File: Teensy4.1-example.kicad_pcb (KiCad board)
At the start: 4 copper layers, 61.5 x 47.5 mm, 80 parts, among them IC1 MIMXRT1062DVJ6B, J1 Conn_01x11_Male, J2 Conn_01x11_Male, J3 Conn_01x12_Male, J4 Conn_01x11_Male, J5 Conn_01x11_Male, J6 Conn_01x03_Male, J7 Conn_01x03_Male, P2 D26, Q1 Q_PMOS_GDS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

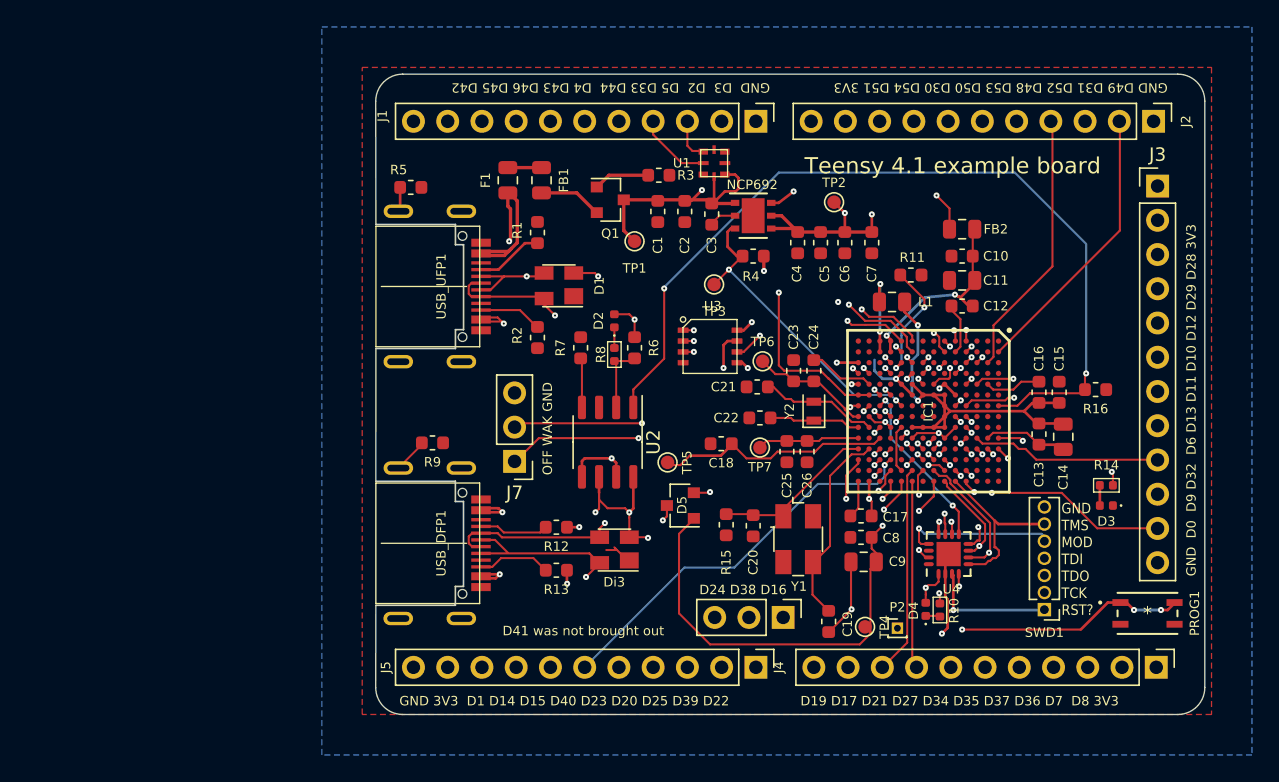
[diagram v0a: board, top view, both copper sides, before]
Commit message: add ARJP11B magjack
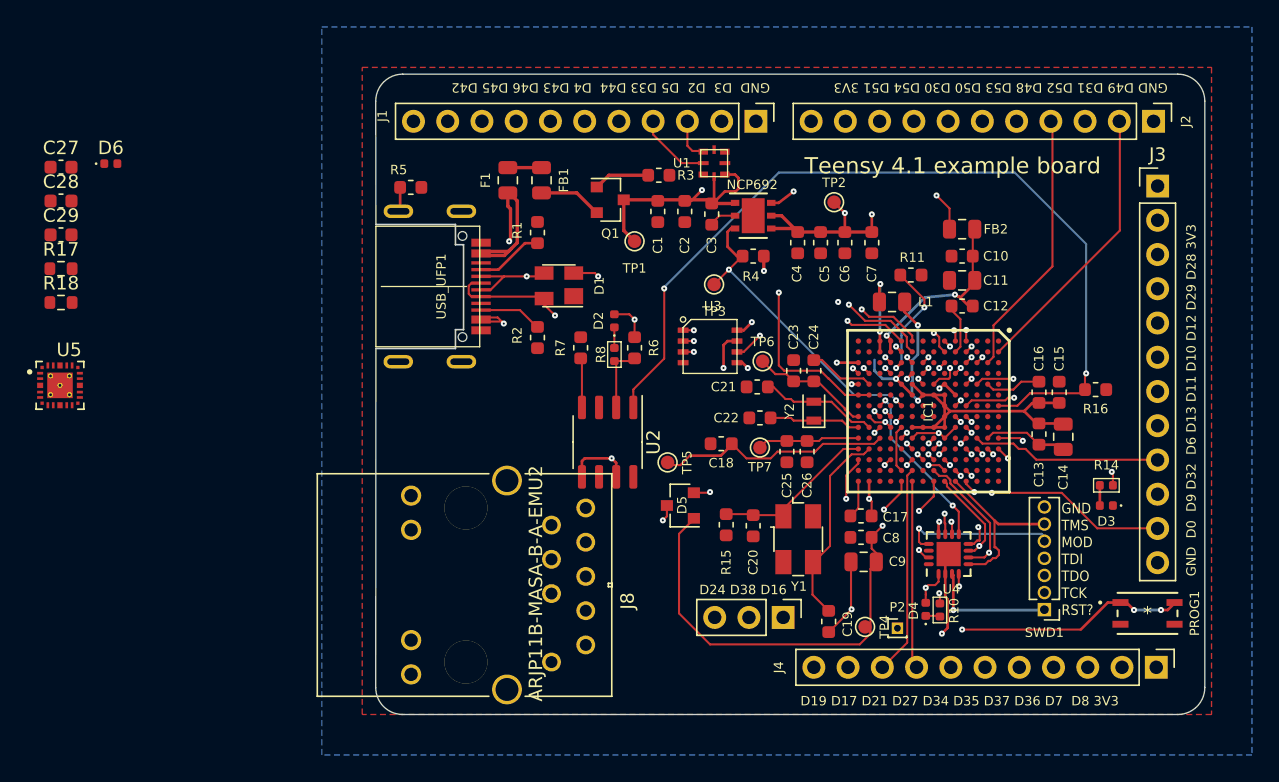
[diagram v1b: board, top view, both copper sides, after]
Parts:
- removed Di3: SP0503BAHT, Package_TO_SOT_SMD:SOT-143
- removed J5: Conn_01x11_Male, Connector_PinHeader_2.54mm:PinHeader_1x11_P2.54mm_Vertical
- removed J7: Conn_01x03_Male, Connector_PinHeader_2.54mm:PinHeader_1x03_P2.54mm_Vertical
- removed R12, R13: 56k, Resistor_SMD:R_0603_1608Metric
- removed R9: 1M, Resistor_SMD:R_0603_1608Metric
- removed USB_DFP1: USB_C_Receptacle_USB2.0, USB-C-Power-tester:TYPE-C-31-M-14
- added C27: 10nf, Capacitor_SMD:C_0603_1608Metric, F.Cu at (29.7, 81.4)
- added C28: 0.22uf, Capacitor_SMD:C_0603_1608Metric, F.Cu at (29.7, 83.9)
- added C29: 2.2uf, Capacitor_SMD:C_0603_1608Metric, F.Cu at (29.7, 86.4)
- added D6: LED, LED_SMD:LED_0402_1005Metric, F.Cu at (33.4, 81.1)
- added J8: ARJP11B-MASA-B-A-EMU2, ARJP11B-MASA-B-A-EMU2:ARJP11B-MASA-B-A-EMU2, F.Cu at (68.6, 106.7)
- added R17: 150, Resistor_SMD:R_0603_1608Metric, F.Cu at (29.7, 88.9)
- added R18: 6.49K, Resistor_SMD:R_0603_1608Metric, F.Cu at (29.7, 91.4)
- added U5: DP83825IRMQR, DP83825IRMQR:XCVR_DP83825IRMQR, F.Cu at (29.6, 97.6)
- Q1: value Q_PMOS_GDS -> Q_PMOS_GDS_DMP3125L
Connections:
- IC1 pad A12: unconnected-(IC1-PadA12) -> /TXD1
- IC1 pad A13: unconnected-(IC1-PadA13) -> /TXEN
- IC1 pad A7: Net-(IC1-PadA7) -> unconnected-(IC1-GPIO_EMC_40-PadA7)
- IC1 pad B12: unconnected-(IC1-PadB12) -> /TXD0
- IC1 pad B13: unconnected-(IC1-PadB13) -> /XI
- IC1 pad B14: unconnected-(IC1-PadB14) -> /MDIO
- IC1 pad C12: unconnected-(IC1-PadC12) -> /DV
- IC1 pad C13: unconnected-(IC1-PadC13) -> /RXER
- IC1 pad C14: unconnected-(IC1-PadC14) -> /MDC
- IC1 pad D12: unconnected-(IC1-PadD12) -> /RXD1
- IC1 pad E10: unconnected-(IC1-PadE10) -> /RST
- IC1 pad E11: unconnected-(IC1-PadE11) -> /INT
- IC1 pad E12: unconnected-(IC1-PadE12) -> /RXD0
- R16 pad 2: Net-(IC1-PadA7) -> Net-(IC1-GPIO_EMC_40)
- U2 pad 1: Net-(IC1-PadA7) -> Net-(IC1-GPIO_EMC_40)
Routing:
- net Net-(IC1-PadA7): track 64.6 -> 0.00 mm, vias 2 -> 0
- net Net-(IC1-GPIO_EMC_40): track 0.00 -> 64.6 mm, vias 0 -> 2
- net /USB2_DP: track 38.4 -> 0.00 mm, vias 2 -> 0
- net /USB2_DN: track 36.5 -> 0.00 mm, vias 2 -> 0
- net /D1: track 36.2 -> 0.00 mm, vias 1 -> 0
- net /D14_A0: track 35.7 -> 0.00 mm, vias 1 -> 0
- net /D15_A1: track 30.8 -> 0.00 mm, vias 1 -> 0
- net /WAKEUP: track 29.6 -> 0.00 mm, vias 2 -> 0
- net /ONOFF: track 29.5 -> 0.00 mm, vias 2 -> 0
- net /D40_A16: track 29.6 -> 0.63 mm
- net /D39_A15: track 26.8 -> 0.00 mm, vias 1 -> 0
- net /D23_A9: track 25.4 -> 0.00 mm, vias 1 -> 0
- net /D20_A6: track 24.9 -> 0.00 mm, vias 1 -> 0
- net Net-(R9-Pad2): track 24.5 -> 0.00 mm
- net /D25_A11: track 23.3 -> 0.00 mm, vias 1 -> 0
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- removed copper zone on In1.Cu, net +5VL
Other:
- outline, holes or cut-outs redrawn
- board text removed: "D41 was not brought out"
- board text removed: "GND 3V3 D1 D14 D15 D40 D23 D20 D25 D39 D22"
- board text removed: "OFF WAK GND"
- board text removed: "Teensy 4.1 example board Feel free to use this as a starting point for your own boards, but pls do the fanout smarter (D41 got trapped and is not broken out). The board includes the required parts - MIMXRT1062DVJ6B (Arm Cortex M7 @ 600 Mhz) - MKL02Z32VFG4 (must be purchased from PJRC) - W25Q64JVXGIM (8Mb spi Flash) Optional parts (not in PJRC's design) - USB Type C for power & debug - USB Type C 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"
